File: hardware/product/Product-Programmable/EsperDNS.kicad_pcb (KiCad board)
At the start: 4 copper layers, 51 x 48 mm, 53 parts, among them J1 USB_B_Micro, J3 RJ45_Amphenol_RJMG1BD3B8K1ANR, Q1 2N7002, Q2 2N7002, Q3 2N7002, Q4 2N7002, Q5 2N7002, SW1 PTS645VH83-2 LFS, U1 AZ1117EH-3.3TRG1, U2 ESP32-WROOM-32E, U3 LAN8720A, U4 CP2102

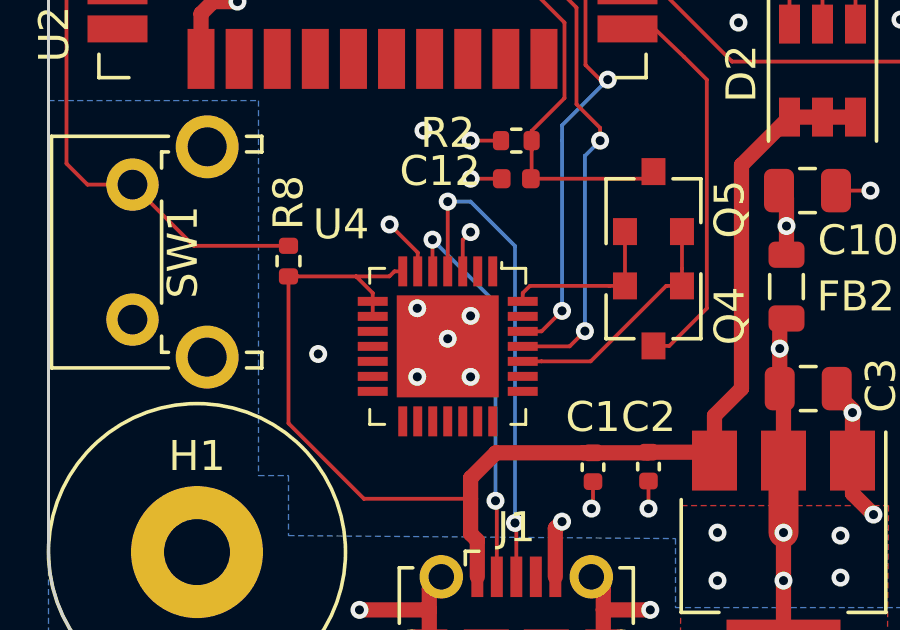
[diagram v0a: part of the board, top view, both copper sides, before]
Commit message: Updated schematic to be more readable
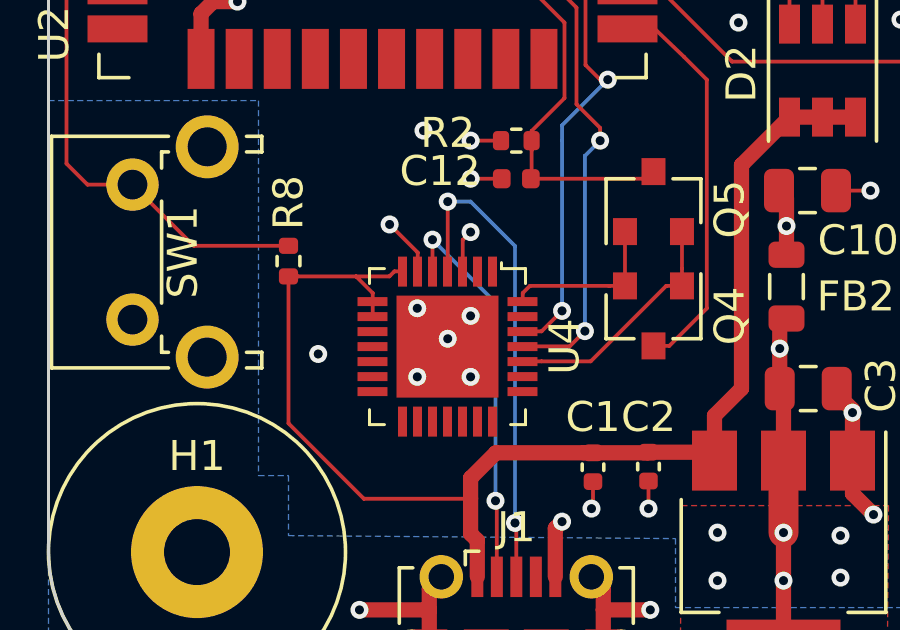
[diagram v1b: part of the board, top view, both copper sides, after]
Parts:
- U4: value CP2102 -> CP2102-GMR_NRND; footprint digikey-footprints:VFQFN-28-1EP_5x5mm -> EsperFootprints:VFQFN-28-1EP_5x5mm
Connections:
- net /ESP32/CLK_R renamed /CLK_R
- net /ESP32/D+ renamed /D+
- net /ESP32/D- renamed /D-
- net /ESP32/TXD0_R renamed /TXD0_R
- net /ESP32/TXD1_R renamed /TXD1_R
- net /ESP32/TXEN_R renamed /TXEN_R
- net /Ethernet/CRS_DV_R renamed /CRS_DV_R
- net /Ethernet/LEDG_K renamed /LEDG_K
- net /Ethernet/LEDY_A renamed /LEDY_A
- net /Ethernet/PHYAD0 renamed /PHYAD0
- net /Ethernet/RBIAS renamed /RBIAS
- net /Ethernet/RD+ renamed /RD+
- net /Ethernet/RD- renamed /RD-
- net /Ethernet/RX0_R renamed /RX0_R
- net /Ethernet/RX1_R renamed /RX1_R
- net /Ethernet/TD+ renamed /TD+
- net /Ethernet/TD- renamed /TD-
- net MTCK renamed /MTCK
- net MTDI renamed /MTDI
- net MTDO renamed /MTDO
- net MTMS renamed /MTMS
